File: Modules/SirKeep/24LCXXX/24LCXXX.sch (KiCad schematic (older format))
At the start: 15 parts, among them J1 Conn_01x05, U1 24LC1025

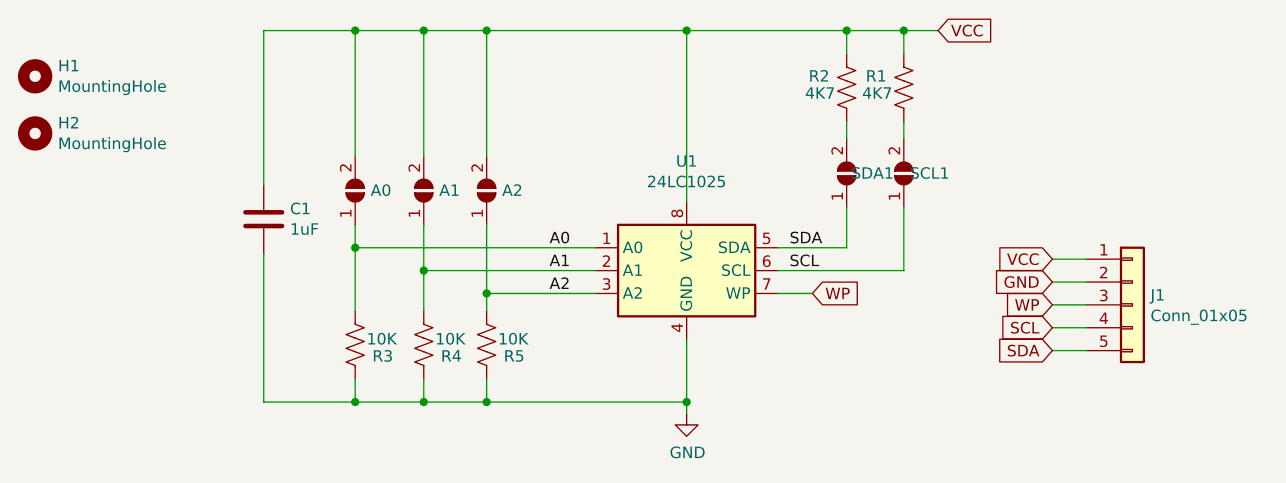
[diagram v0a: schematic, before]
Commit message: 24LCXXX Added in place of 24512
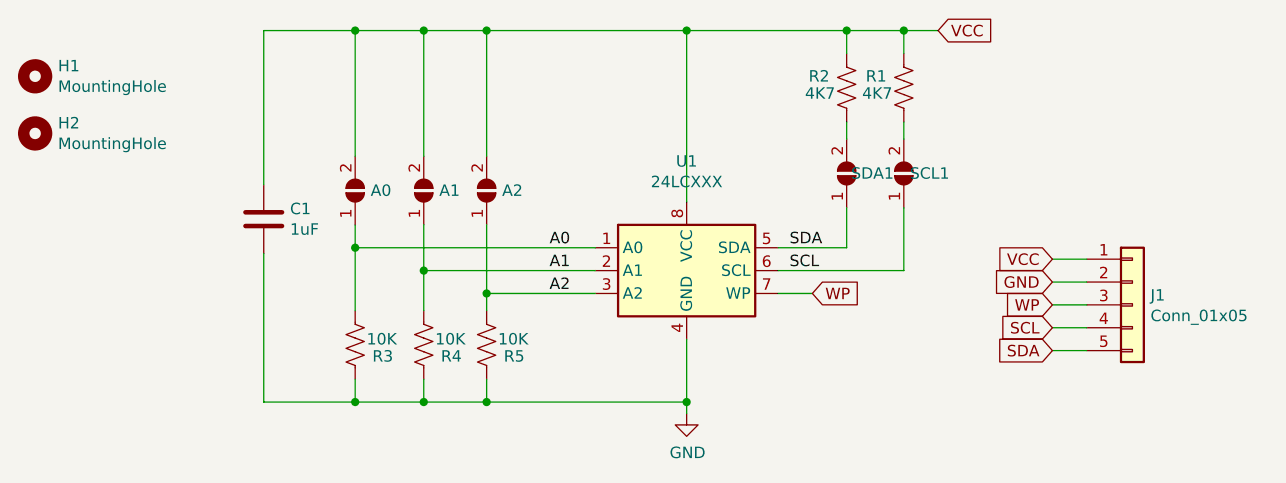
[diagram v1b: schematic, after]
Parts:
- U1: value 24LC1025 -> 24LCXXX
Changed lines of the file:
@@
 encoding utf-8
 Sheet 1 1
-Title "24LC512 Based EEPROM Module"
+Title "24LCXXX Based EEPROM Module"
 Date "2019-12-05"
 Rev "1"
@@
 Comment1 "SirBoard"
 Comment2 "SirKeep"
-Comment3 "24LC512"
+Comment3 "24LC64, 24LC128, 24LC256, 24LC512, 24LC1024"
 Comment4 ""
 $EndDescr
@@
 P 4300 2200
 F 0 "U1" H 4300 2678 50  0000 C CNN
-F 1 "24LC1025" H 4300 2588 50  0000 C CNN
+F 1 "24LCXXX" H 4300 2588 50  0000 C CNN
 F 2 "Package_SO:SOIC-8_3.9x4.9mm_P1.27mm" H 4300 2200 50  0001 C CNN
 F 3 "http://ww1.microchip.com/downloads/en/DeviceDoc/21941B.pdf" H 4300 2200 50  0001 C CNN
